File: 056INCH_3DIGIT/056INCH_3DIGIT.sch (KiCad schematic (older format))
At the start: 1 part

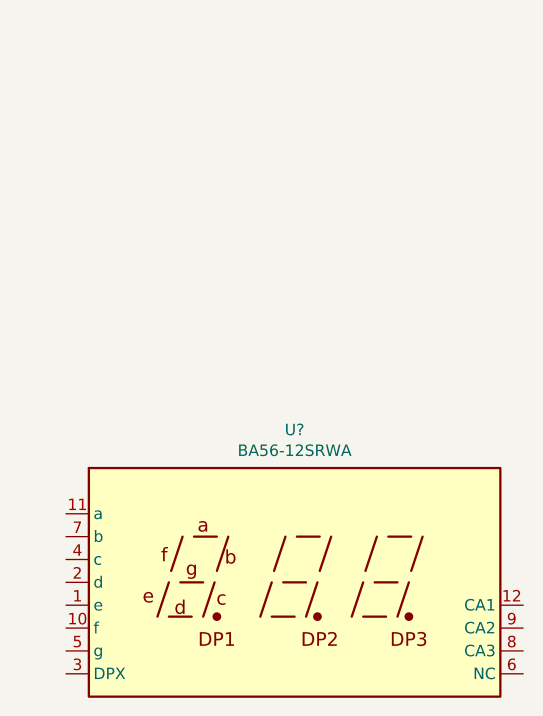
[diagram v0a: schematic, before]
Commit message: 3 digit display symbol & footprint finished
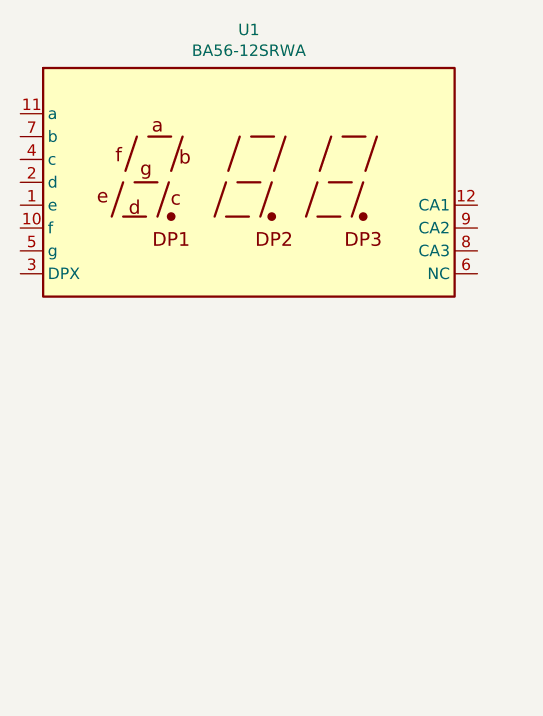
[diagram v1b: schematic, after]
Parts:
- removed U?: BA56-12SRWA, KINGBRIGHTUSA:BA56-12SRWA, symbol kingbrightusa:BA56-12SRWA
- added U1: BA56-12SRWA, KINGBRIGHTUSA:BA56-12SRWA, symbol kingbrightusa:BA56-12SRWA
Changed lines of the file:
@@
 $EndDescr
 $Comp
-L kingbrightusa:BA56-12SRWA U?
-U 1 1 618E4546
-P 5650 5750
-F 0 "U?" H 5650 6417 50  0000 C CNN
-F 1 "BA56-12SRWA" H 5650 6326 50  0000 C CNN
-F 2 "KINGBRIGHTUSA:BA56-12SRWA" H 5650 5150 50  0001 C CNN
-F 3 "https://www.kingbrightusa.com/images/catalog/SPEC/BA56-12SRWA.pdf" H 5220 5780 50  0001 C CNN
-	1    5650 5750
+L kingbrightusa:BA56-12SRWA U1
+U 1 1 618EFA42
+P 5450 4000
+F 0 "U1" H 5450 4667 50  0000 C CNN
+F 1 "BA56-12SRWA" H 5450 4576 50  0000 C CNN
+F 2 "KINGBRIGHTUSA:BA56-12SRWA" H 5450 3400 50  0001 C CNN
+F 3 "https://www.kingbrightusa.com/images/catalog/SPEC/BA56-12SRWA.pdf" H 5020 4030 50  0001 C CNN
+	1    5450 4000
 	1    0    0    -1
 $EndComp

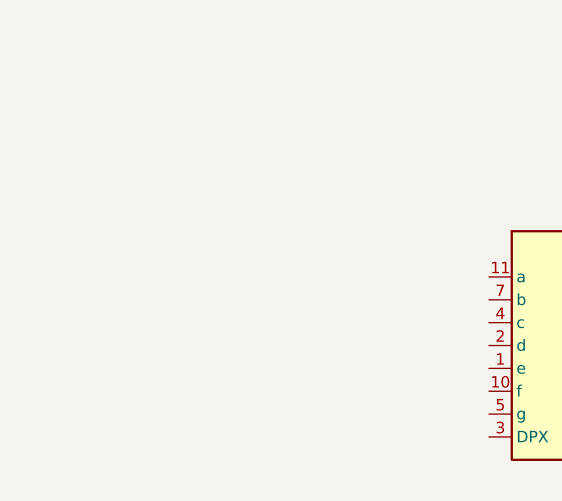
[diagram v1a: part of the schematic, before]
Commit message: TM1637 symbol finished
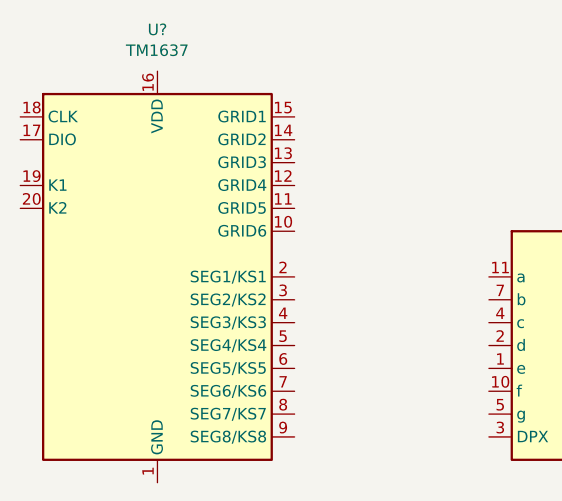
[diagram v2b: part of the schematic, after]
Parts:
- added U?: TM1637, Package_SO:SO-20_12.8x7.5mm_P1.27mm, symbol titanmicroelectronics:TM1637
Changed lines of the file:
@@
+	1    0    0    -1
+$EndComp
+$Comp
+L titanmicroelectronics:TM1637 U?
+U 1 1 618E730A
+P 3000 3700
+F 0 "U?" H 3000 4781 50  0000 C CNN
+F 1 "TM1637" H 3000 4690 50  0000 C CNN
+F 2 "Package_SO:SO-20_12.8x7.5mm_P1.27mm" H 3200 4000 50  0001 C CNN
+F 3 "https://www.mcielectronics.cl/website_MCI/static/documents/Datasheet_TM1637.pdf" H 3200 4000 50  0001 C CNN
+	1    3000 3700
 	1    0    0    -1
 $EndComp

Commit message: first connections schematic
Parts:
- gave numbers to parts that had none: 1
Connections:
- net at U2.13 (GRID3): now also U1.8 (CA3)
- net at U2.14 (GRID2): now also U1.9 (CA2)
- net at U2.15 (GRID1): now also U1.12 (CA1)
- net at U2.2 (SEG1/KS1): now also U1.11 (a)
- net at U2.3 (SEG2/KS2): now also U1.7 (b)
- net at U2.4 (SEG3/KS3): now also U1.4 (c)
- net at U2.5 (SEG4/KS4): now also U1.2 (d)
- net at U2.6 (SEG5/KS5): now also U1.1 (e)
- net at U2.7 (SEG6/KS6): now also U1.10 (f)
- net at U2.8 (SEG7/KS7): now also U1.5 (g)
- net at U2.9 (SEG8/KS8): now also U1.3 (DPX)
- no-connect marks 0 -> 3
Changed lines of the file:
@@
 $EndComp
 $Comp
-L titanmicroelectronics:TM1637 U?
+L titanmicroelectronics:TM1637 U2
 U 1 1 618E730A
 P 3000 3700
-F 0 "U?" H 3000 4781 50  0000 C CNN
+F 0 "U2" H 3000 4781 50  0000 C CNN
 F 1 "TM1637" H 3000 4690 50  0000 C CNN
 F 2 "Package_SO:SO-20_12.8x7.5mm_P1.27mm" H 3200 4000 50  0001 C CNN
@@
 	1    0    0    -1
 $EndComp
+Wire Wire Line
+	3600 3700 4450 3700
+Wire Wire Line
+	3600 3800 4450 3800
+Wire Wire Line
+	3600 3900 4450 3900
+Wire Wire Line
+	3600 4000 4450 4000
+Wire Wire Line
+	3600 4100 4450 4100
+Wire Wire Line
+	3600 4200 4450 4200
+Wire Wire Line
+	3600 4300 4450 4300
+Wire Wire Line
+	3600 4400 4450 4400
+Wire Wire Line
+	6450 4300 6800 4300
+Wire Wire Line
+	6450 4200 6700 4200
+Wire Wire Line
+	6450 4100 6600 4100
+Wire Wire Line
+	3600 3000 6600 3000
+Wire Wire Line
+	6600 3000 6600 4100
+Wire Wire Line
+	3600 3100 6700 3100
+Wire Wire Line
+	6700 3100 6700 4200
+Wire Wire Line
+	3600 3200 6800 3200
+Wire Wire Line
+	6800 3200 6800 4300
+NoConn ~ 3600 3300
+NoConn ~ 3600 3400
+NoConn ~ 3600 3500
 $EndSCHEMATC

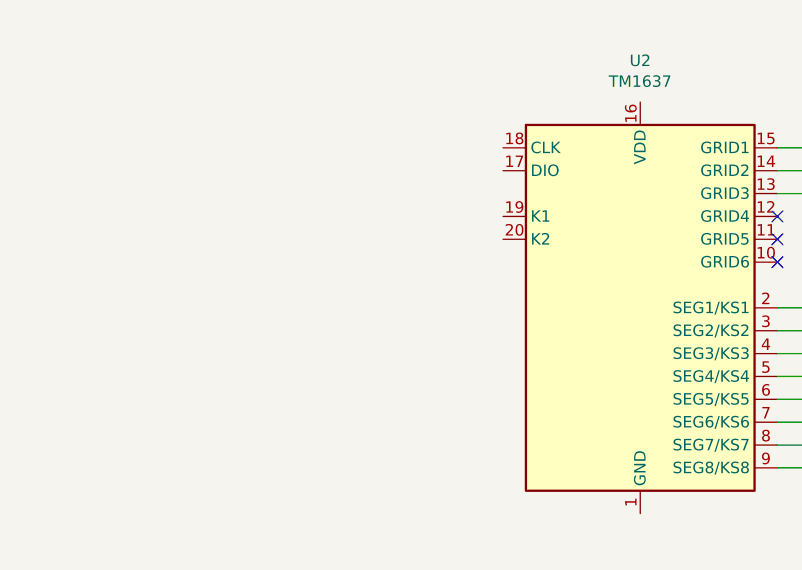
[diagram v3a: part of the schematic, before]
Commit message: all traces routed
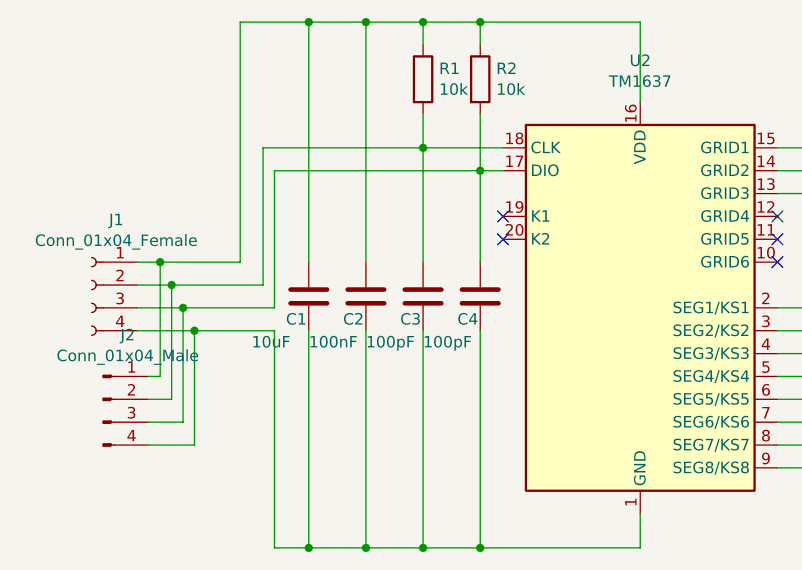
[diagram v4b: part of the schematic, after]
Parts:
- added C1: 10uF, Capacitor_SMD:C_0805_2012Metric_Pad1.15x1.40mm_HandSolder, symbol Device:C
- added C2: 100nF, Capacitor_SMD:C_0805_2012Metric_Pad1.15x1.40mm_HandSolder, symbol Device:C
- added C3, C4: 100pF, Capacitor_SMD:C_0805_2012Metric_Pad1.15x1.40mm_HandSolder, symbol Device:C
- added J1: Conn_01x04_Female, TerminalBlock_4Ucon:TerminalBlock_4Ucon_1x04_P3.50mm_Horizontal, symbol Connector:Conn_01x04_Female
- added J2: Conn_01x04_Male, Connector_PinHeader_2.54mm:PinHeader_1x04_P2.54mm_Vertical, symbol Connector:Conn_01x04_Male
- added R1, R2: 10k, Resistor_SMD:R_0805_2012Metric_Pad1.15x1.40mm_HandSolder, symbol Device:R
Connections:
- net at U2.1 (GND): now also C1.2, C2.2, C3.2, C4.2, J1.4 (Pin_4), J2.4 (Pin_4)
- net at U2.16 (VDD): now also C1.1, C2.1, J1.1 (Pin_1), J2.1 (Pin_1), R1.1, R2.1
- net at U2.17 (DIO): now also C4.1, J1.3 (Pin_3), J2.3 (Pin_3), R2.2
- net at U2.18 (CLK): now also C3.1, J1.2 (Pin_2), J2.2 (Pin_2), R1.2
- no-connect marks 3 -> 5
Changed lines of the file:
@@
 NoConn ~ 3600 3400
 NoConn ~ 3600 3500
+$Comp
+L Connector:Conn_01x04_Female J1
+U 1 1 618E9513
+P 600 3600
+F 0 "J1" H 492 3885 50  0000 C CNN
+F 1 "Conn_01x04_Female" H 492 3794 50  0000 C CNN
+F 2 "TerminalBlock_4Ucon:TerminalBlock_4Ucon_1x04_P3.50mm_Horizontal" H 600 3600 50  0001 C CNN
+F 3 "~" H 600 3600 50  0001 C CNN
+	1    600  3600
+	-1   0    0    -1
+$EndComp
+Wire Wire Line
+	3000 2450 3000 2800
+Wire Wire Line
+	3000 4750 3000 4600
+NoConn ~ 2400 3400
+NoConn ~ 2400 3300
+$Comp
+L Device:C C4
+U 1 1 618F3C54
+P 2300 3650
+F 0 "C4" H 2200 3550 50  0000 L CNN
+F 1 "100pF" H 2050 3450 50  0000 L CNN
+F 2 "Capacitor_SMD:C_0805_2012Metric_Pad1.15x1.40mm_HandSolder" H 2338 3500 50  0001 C CNN
+F 3 "~" H 2300 3650 50  0001 C CNN
+	1    2300 3650
+	1    0    0    -1
+$EndComp
+$Comp
+L Device:C C3
+U 1 1 618F4017
+P 2050 3650
+F 0 "C3" H 1950 3550 50  0000 L CNN
+F 1 "100pF" H 1800 3450 50  0000 L CNN
+F 2 "Capacitor_SMD:C_0805_2012Metric_Pad1.15x1.40mm_HandSolder" H 2088 3500 50  0001 C CNN
+F 3 "~" H 2050 3650 50  0001 C CNN
+	1    2050 3650
+	1    0    0    -1
+$EndComp
+$Comp
+L Device:C C2
+U 1 1 618F43A8
+P 1800 3650
+F 0 "C2" H 1700 3550 50  0000 L CNN
+F 1 "100nF" H 1550 3450 50  0000 L CNN
+F 2 "Capacitor_SMD:C_0805_2012Metric_Pad1.15x1.40mm_HandSolder" H 1838 3500 50  0001 C CNN
+F 3 "~" H 1800 3650 50  0001 C CNN
+	1    1800 3650
+	1    0    0    -1
+$EndComp
+$Comp
+L Device:C C1
+U 1 1 618F4787
+P 1550 3650
+F 0 "C1" H 1450 3550 50  0000 L CNN
+F 1 "10uF" H 1300 3450 50  0000 L CNN
+F 2 "Capacitor_SMD:C_0805_2012Metric_Pad1.15x1.40mm_HandSolder" H 1588 3500 50  0001 C CNN
+F 3 "~" H 1550 3650 50  0001 C CNN
+	1    1550 3650
+	1    0    0    -1
+$EndComp
+Wire Wire Line
+	2300 3800 2300 4750
+Connection ~ 2300 4750
+Wire Wire Line
+	2300 4750 3000 4750
+Wire Wire Line
+	2050 4750 2300 4750
+Wire Wire Line
+	2400 3100 2300 3100
+Wire Wire Line
+	2300 3100 2300 3500
+Wire Wire Line
+	2400 3000 2050 3000
+Wire Wire Line
+	2050 3000 2050 3500
+Wire Wire Line
+	2050 3800 2050 4750
+$Comp
+L Device:R R2
+U 1 1 618FC30B
+P 2300 2700
+F 0 "R2" H 2370 2746 50  0000 L CNN
+F 1 "10k" H 2370 2655 50  0000 L CNN
+F 2 "Resistor_SMD:R_0805_2012Metric_Pad1.15x1.40mm_HandSolder" V 2230 2700 50  0001 C CNN
+F 3 "~" H 2300 2700 50  0001 C CNN
+	1    2300 2700
+	1    0    0    -1
+$EndComp
+$Comp
+L Device:R R1
+U 1 1 618FD638
+P 2050 2700
+F 0 "R1" H 2120 2746 50  0000 L CNN
+F 1 "10k" H 2120 2655 50  0000 L CNN
+F 2 "Resistor_SMD:R_0805_2012Metric_Pad1.15x1.40mm_HandSolder" V 1980 2700 50  0001 C CNN
+F 3 "~" H 2050 2700 50  0001 C CNN
+	1    2050 2700
+	1    0    0    -1
+$EndComp
+Wire Wire Line
+	2300 3100 2300 2850
+Connection ~ 2300 3100
+Wire Wire Line
+	2050 3000 2050 2850
+Connection ~ 2050 3000
+Wire Wire Line
+	2300 2550 2300 2450
+Connection ~ 2300 2450
+Wire Wire Line
+	2300 2450 3000 2450
+Wire Wire Line
+	2050 2550 2050 2450
+Wire Wire Line
+	2050 2450 2300 2450
+Wire Wire Line
+	1250 3500 1250 2450
+Wire Wire Line
+	1250 2450 1550 2450
+Connection ~ 2050 2450
+Connection ~ 2050 4750
+Wire Wire Line
+	1800 3800 1800 4750
+Connection ~ 1800 4750
+Wire Wire Line
+	1800 4750 2050 4750
+Wire Wire Line
+	1550 3800 1550 4750
+Connection ~ 1550 4750
+Wire Wire Line
+	1550 4750 1800 4750
+Wire Wire Line
+	1800 3500 1800 2450
+Connection ~ 1800 2450
+Wire Wire Line
+	1800 2450 2050 2450
+Wire Wire Line
+	1550 3500 1550 2450
+Connection ~ 1550 2450
+Wire Wire Line
+	1550 2450 1800 2450
+Wire Wire Line
+	1350 3600 1350 3000
+Wire Wire Line
+	1350 3000 2050 3000
+Wire Wire Line
+	1400 3700 1400 3100
+Wire Wire Line
+	1400 3100 2300 3100
+Wire Wire Line
+	1400 3800 1400 4750
+Wire Wire Line
+	1400 4750 1550 4750
+Wire Wire Line
+	800  3800 1050 3800
+Wire Wire Line
+	800  3700 1000 3700
+Wire Wire Line
+	800  3600 950  3600
+Wire Wire Line
+	800  3500 900  3500
+$Comp
+L Connector:Conn_01x04_Male J2
+U 1 1 619257D5
+P 650 4100
+F 0 "J2" H 758 4381 50  0000 C CNN
+F 1 "Conn_01x04_Male" H 758 4290 50  0000 C CNN
+F 2 "Connector_PinHeader_2.54mm:PinHeader_1x04_P2.54mm_Vertical" H 650 4100 50  0001 C CNN
+F 3 "~" H 650 4100 50  0001 C CNN
+	1    650  4100
+	1    0    0    -1
+$EndComp
+Wire Wire Line
+	850  4000 900  4000
+Wire Wire Line
+	900  4000 900  3500
+Connection ~ 900  3500
+Wire Wire Line
+	900  3500 1250 3500
+Wire Wire Line
+	850  4100 950  4100
+Wire Wire Line
+	950  4100 950  3600
+Connection ~ 950  3600
+Wire Wire Line
+	950  3600 1350 3600
+Wire Wire Line
+	850  4200 1000 4200
+Wire Wire Line
+	1000 4200 1000 3700
+Connection ~ 1000 3700
+Wire Wire Line
+	1000 3700 1400 3700
+Wire Wire Line
+	850  4300 1050 4300
+Wire Wire Line
+	1050 4300 1050 3800
+Connection ~ 1050 3800
+Wire Wire Line
+	1050 3800 1400 3800
 $EndSCHEMATC
